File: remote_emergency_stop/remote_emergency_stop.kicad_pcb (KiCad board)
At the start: 2 copper layers, 1 part, among them U1 MOUDLE-SEEEDUINO-XIAO-ESP32C3

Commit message: こりゃだめだ、ユーザーインタフェイスが整ってない。
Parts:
- added D1: LED, LED_SMD:LED_0603_1608Metric_Pad1.05x0.95mm_HandSolder, F.Cu at (127.5, 147.0)
- added D2: LED, LED_SMD:LED_0603_1608Metric_Pad1.05x0.95mm_HandSolder, F.Cu at (135.0, 147.0)
- added D3: LED, LED_SMD:LED_0603_1608Metric_Pad1.05x0.95mm_HandSolder, F.Cu at (143.0, 146.9)
- added D4: LED, LED_SMD:LED_0603_1608Metric_Pad1.05x0.95mm_HandSolder, F.Cu at (150.0, 147.0)
- added D5: LED, LED_SMD:LED_0603_1608Metric_Pad1.05x0.95mm_HandSolder, F.Cu at (157.0, 138.0)
- added J1: Conn_01x02, Connector_JST:JST_XH_S2B-XH-A_1x02_P2.50mm_Horizontal, F.Cu at (148.2, 127.5)
- added R3: 1K, Resistor_SMD:R_0603_1608Metric_Pad0.98x0.95mm_HandSolder, F.Cu at (127.5, 143.0)
- added R4: 1K, Resistor_SMD:R_0603_1608Metric_Pad0.98x0.95mm_HandSolder, F.Cu at (135.0, 143.0)
- added R5: 1K, Resistor_SMD:R_0603_1608Metric_Pad0.98x0.95mm_HandSolder, F.Cu at (143.0, 142.9)
- added R6: 1K, Resistor_SMD:R_0603_1608Metric_Pad0.98x0.95mm_HandSolder, F.Cu at (150.0, 143.0)
- added R7: 500, Resistor_SMD:R_0603_1608Metric_Pad0.98x0.95mm_HandSolder, F.Cu at (153.0, 138.1)
- added REF**: MountingHole_3.2mm_M3, MountingHole:MountingHole_3.2mm_M3, F.Cu at (120.0, 146.0)
- added REF**: MountingHole_3.2mm_M3, MountingHole:MountingHole_3.2mm_M3, F.Cu at (156.0, 121.0)
- added REF**: MountingHole_3.2mm_M3, MountingHole:MountingHole_3.2mm_M3, F.Cu at (156.0, 146.0)
- moved U1 40.3 mm to (128.4, 129.1), turned to 90 degrees
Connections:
- U1 pad 1: unconnected-(U1-PA02_A0_D0-Pad1) -> LED1
- U1 pad 11: unconnected-(U1-PA6_A10_D10_MOSI-Pad11) -> ENABLE
- U1 pad 12: unconnected-(U1-3V3-Pad12) -> +3.3V
- U1 pad 13: unconnected-(U1-GND-Pad13) -> GND
- U1 pad 14: unconnected-(U1-5V-Pad14) -> +5V
- U1 pad 2: unconnected-(U1-PA4_A1_D1-Pad2) -> LED2
- U1 pad 3: unconnected-(U1-PA10_A2_D2-Pad3) -> LED3
- U1 pad 4: unconnected-(U1-PA11_A3_D3-Pad4) -> LED4
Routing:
- added copper zone on B.Cu, net GND
- added copper zone on F.Cu, net GND
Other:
- board outline added: 44 x 33 mm

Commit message: 遠隔非常停止は回路だけ完成した気がする
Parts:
- removed D4, D5: LED, LED_SMD:LED_0603_1608Metric_Pad1.05x0.95mm_HandSolder
- removed REF** (x3): MountingHole_3.2mm_M3, MountingHole:MountingHole_3.2mm_M3
- added BZ1: Buzzer, Buzzer_Beeper:Buzzer_12x9.5RM7.6, F.Cu at (149.4, 144.0)
- added J2: Conn_01x02, Connector_JST:JST_XH_S2B-XH-A_1x02_P2.50mm_Horizontal, F.Cu at (140.4, 140.6)
- added Q1: BSS138, Package_TO_SOT_SMD:SOT-23, F.Cu at (153.0, 133.7)
- added R1: 220K, Resistor_SMD:R_0603_1608Metric, F.Cu at (152.6, 114.4)
- added R10: 1K, Resistor_SMD:R_0603_1608Metric, F.Cu at (156.6, 124.5)
- added R2: 220K, Resistor_SMD:R_0603_1608Metric, F.Cu at (152.6, 116.9)
- added R8: 500, Resistor_SMD:R_0603_1608Metric, F.Cu at (156.6, 119.5)
- added R9: 1K, Resistor_SMD:R_0603_1608Metric, F.Cu at (156.6, 122.0)
- added SW1: SW_DIP_x02, Button_Switch_SMD:SW_DIP_SPSTx02_Slide_Omron_A6H-2101_W6.15mm_P1.27mm, F.Cu at (155.1, 128.5)
- D1: value LED -> Yellow
- D2: value LED -> Blue
- D3: value LED -> Red
- R3, R4, R5: value 1K -> 10K; footprint Resistor_SMD:R_0603_1608Metric_Pad0.98x0.95mm_HandSolder -> Resistor_SMD:R_0603_1608Metric
- R6: footprint Resistor_SMD:R_0603_1608Metric_Pad0.98x0.95mm_HandSolder -> Resistor_SMD:R_0603_1608Metric
- R7: value 500 -> 20K; footprint Resistor_SMD:R_0603_1608Metric_Pad0.98x0.95mm_HandSolder -> Resistor_SMD:R_0603_1608Metric
- moved D1 46.6 mm to (160.8, 114.5), turned to 0 degrees
- moved D2 39.5 mm to (160.8, 117.1), turned to 0 degrees
- moved R3 34.4 mm to (152.6, 119.5), turned to 0 degrees
- moved R6 29.3 mm to (156.6, 114.4), turned to 0 degrees
- moved R4 27.4 mm to (152.6, 122.0), turned to 0 degrees
- moved D3 21.7 mm to (161.1, 135.0), turned to 0 degrees
- moved J1 21.7 mm to (131.0, 140.6), turned to 0 degrees
- moved R7 21.5 mm to (156.6, 116.9)
- moved R5 20.7 mm to (152.6, 124.5), turned to 0 degrees
- moved U1 11.2 mm to (139.1, 125.7), turned to 0 degrees
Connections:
- D1 pad 1: GND -> Net-(BZ1--)
- R3 pad 1: LED1 -> DIP1
- R3 pad 2: Net-(D1-A) -> GND
- R4 pad 1: LED2 -> DIP2
- R4 pad 2: Net-(D2-A) -> GND
- R5 pad 1: LED3 -> GND
- R5 pad 2: Net-(D3-A) -> SW
- R6 pad 1: LED4 -> ENABLE
- R6 pad 2: Net-(D4-A) -> Net-(Q1-G)
- R7 pad 1: ENABLE -> Net-(Q1-G)
- R7 pad 2: Net-(D5-A) -> GND
- U1 pad 1: LED1 -> BAT_LEVEL
- U1 pad 11: ENABLE -> unconnected-(U1-PA6_A10_D10_MOSI-Pad11)
- U1 pad 2: LED2 -> WIRELESS
- U1 pad 3: LED3 -> ENABLE
- U1 pad 4: LED4 -> DIP1
- U1 pad 5: unconnected-(U1-PA8_A4_D4_SDA-Pad5) -> DIP2
- U1 pad 6: unconnected-(U1-PA9_A5_D5_SCL-Pad6) -> SW
- U1 pad 8: unconnected-(U1-PB09_A7_D7_RX-Pad8) -> BAT_LOW
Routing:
- removed copper zone on B.Cu, net GND
- removed copper zone on F.Cu, net GND
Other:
- board outline removed

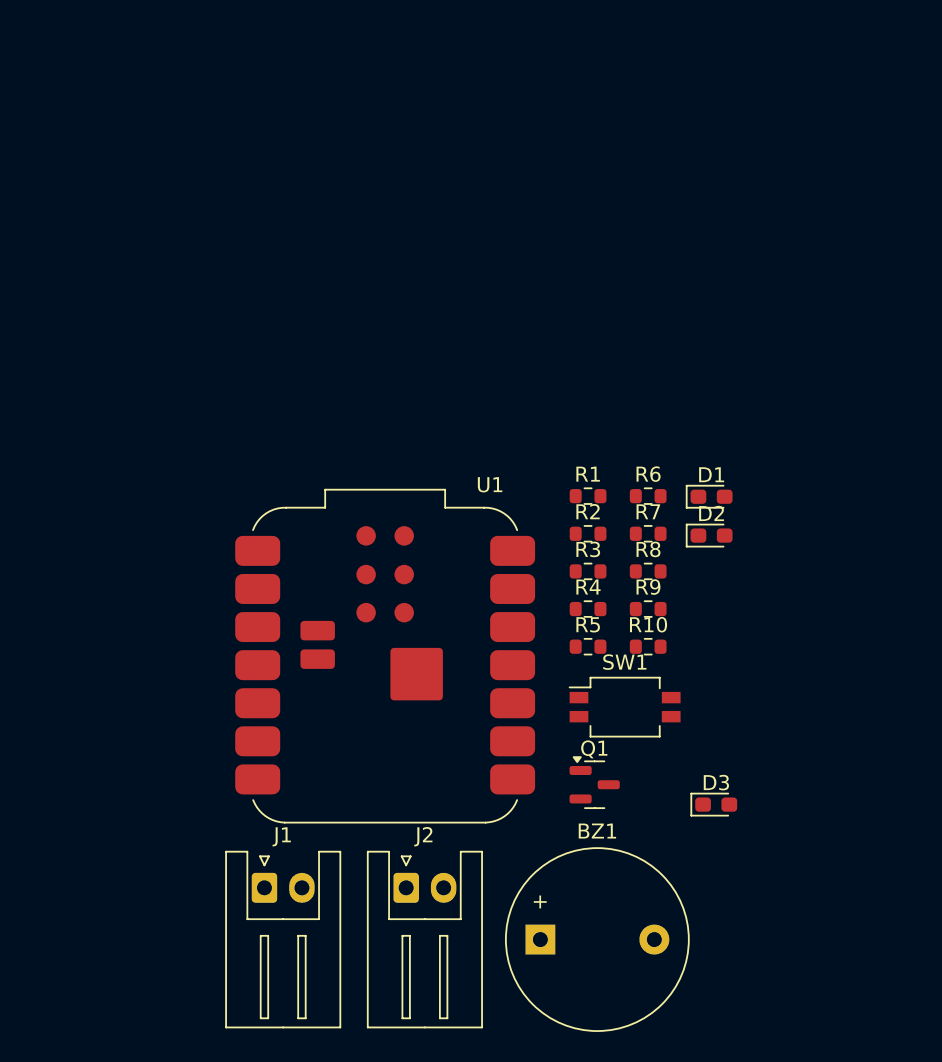
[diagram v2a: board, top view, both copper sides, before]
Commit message: 遠隔非常停止のフットプリント決定した。回路にコンデンサ追加
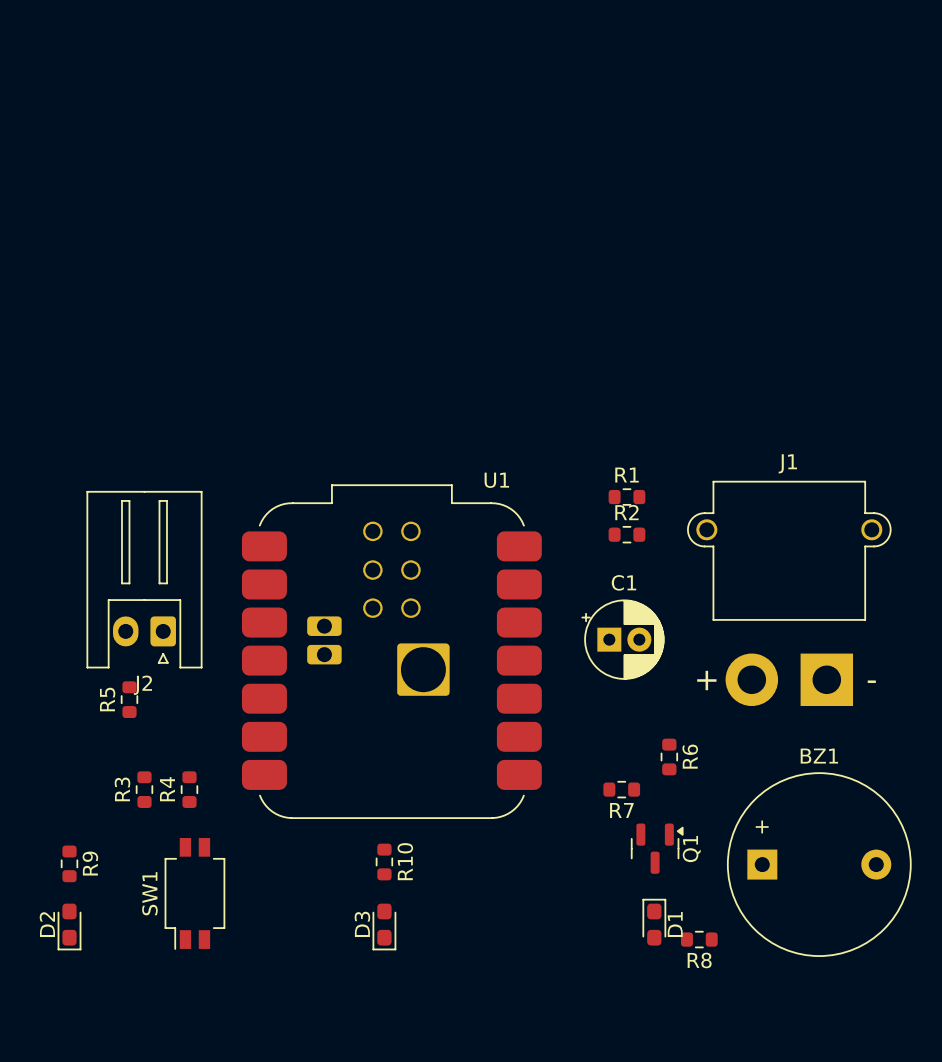
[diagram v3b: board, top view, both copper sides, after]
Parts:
- added C1: 100uF, Capacitor_THT:CP_Radial_D5.0mm_P2.00mm, F.Cu at (154.0, 124.0)
- J1: footprint Connector_JST:JST_XH_S2B-XH-A_1x02_P2.50mm_Horizontal -> Connector_AMASS:AMASS_XT30PW-M_1x02_P2.50mm_Horizontal
- moved D2 50.1 mm to (118.0, 143.0), turned to 90 degrees
- moved R9 42.2 mm to (118.0, 138.9), turned to -90 degrees
- moved J1 40.0 mm to (168.5, 126.7)
- moved R3 33.0 mm to (123.0, 134.0), turned to 90 degrees
- moved SW1 31.3 mm to (126.4, 140.9), turned to 90 degrees
- moved R5 30.8 mm to (122.0, 128.0), turned to 90 degrees
- moved R4 29.2 mm to (126.0, 134.0), turned to 90 degrees
- moved D1 28.8 mm to (157.0, 143.0), turned to -90 degrees
- moved R8 24.8 mm to (160.0, 144.0), turned to 180 degrees
- moved J2 23.6 mm to (124.2, 123.5), turned to 180 degrees
- moved D3 23.5 mm to (139.0, 143.0), turned to 90 degrees
- moved R10 22.7 mm to (139.0, 138.8), turned to -90 degrees
- moved R6 17.5 mm to (158.0, 131.8), turned to -90 degrees
- moved R7 17.2 mm to (154.8, 134.0), turned to 180 degrees
- moved BZ1 15.6 mm to (164.2, 139.0)
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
